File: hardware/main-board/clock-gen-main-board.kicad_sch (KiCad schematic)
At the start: 10 parts, among them J1 Conn_01x03_Pin, J2 Conn_01x03_Pin, J3 Conn_01x03_Pin, U1 Pico

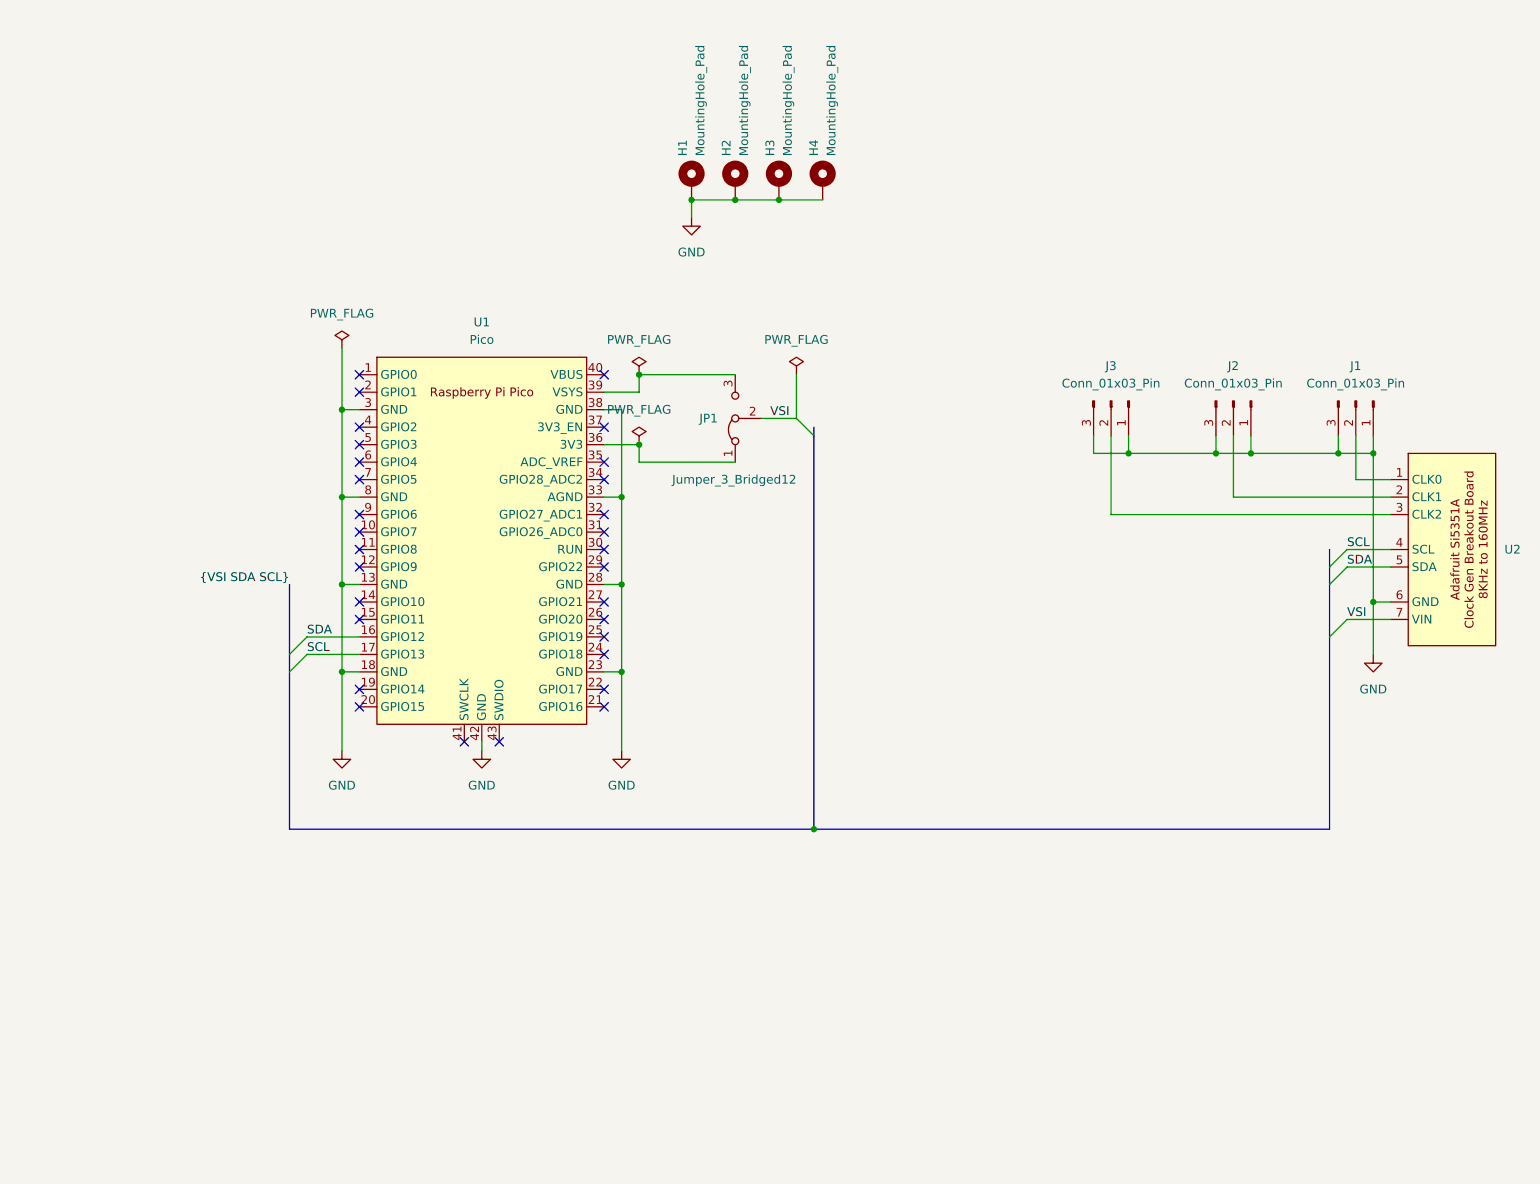
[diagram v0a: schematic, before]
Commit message: Resolve "Extend mainboard with audio ADC"
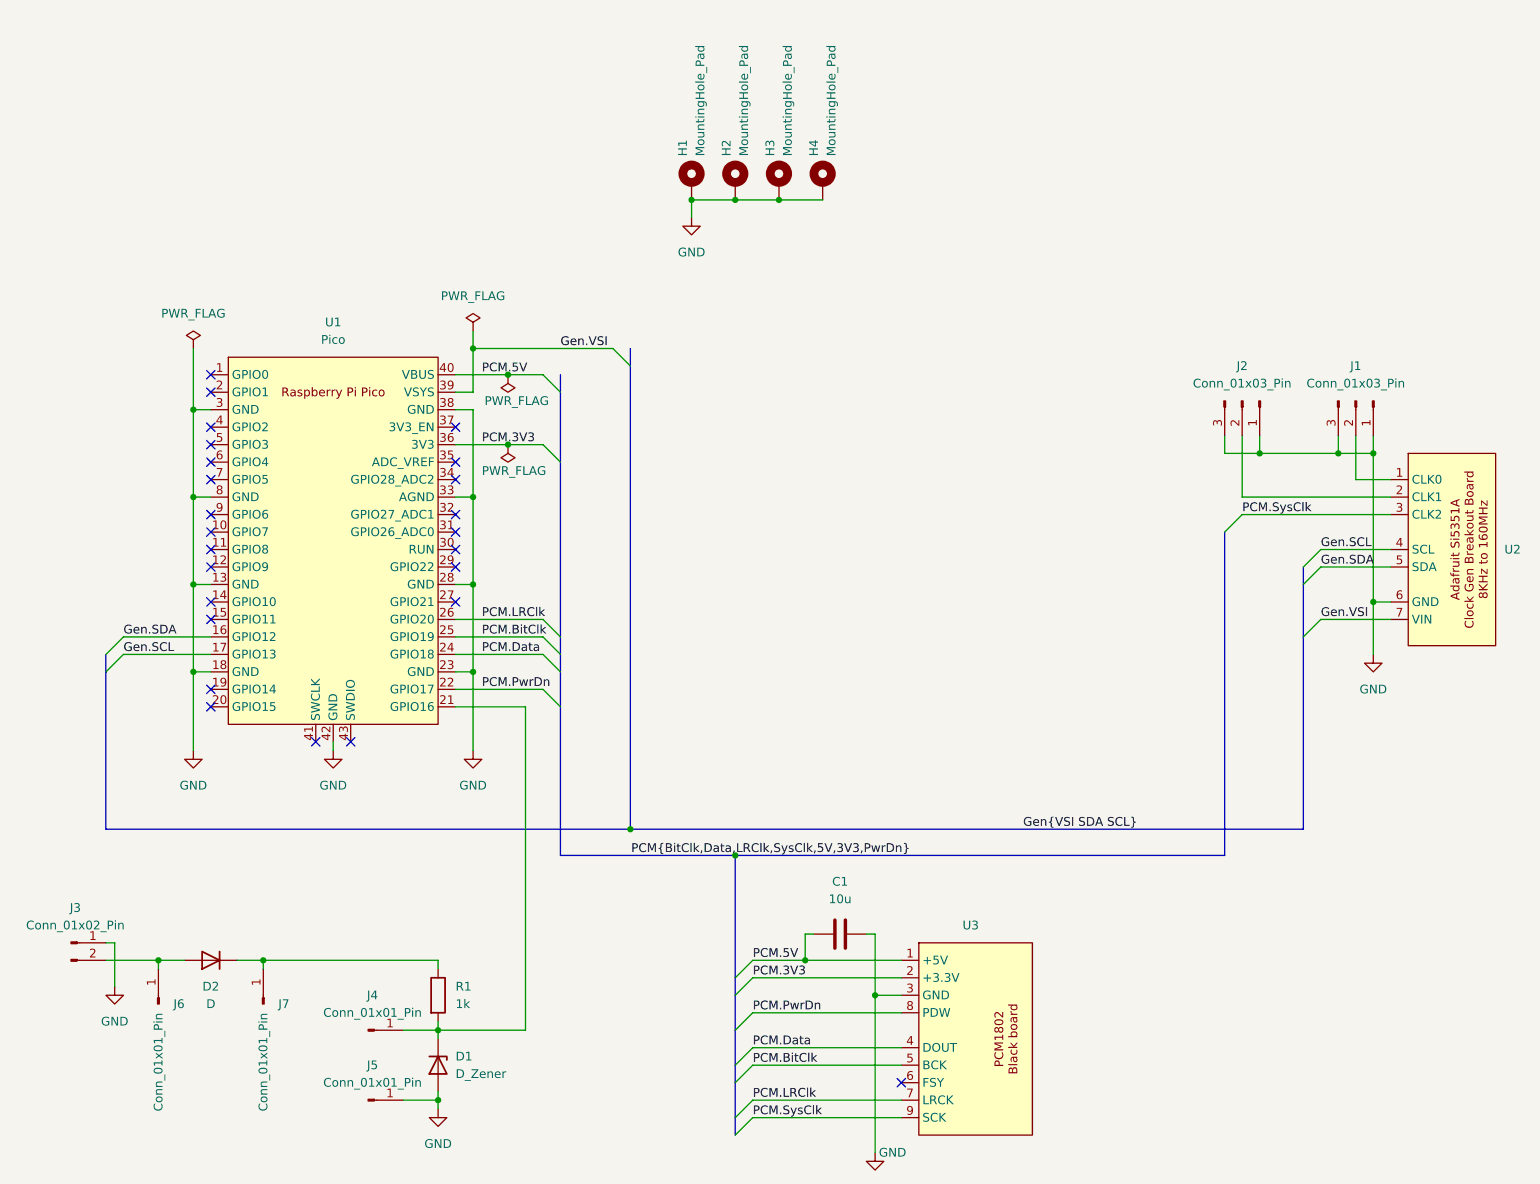
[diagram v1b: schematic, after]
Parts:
- removed J3: Conn_01x03_Pin, Connector_PinHeader_2.54mm:PinHeader_1x03_P2.54mm_Vertical, symbol Connector:Conn_01x03_Pin
- removed JP1: Jumper_3_Bridged12, Connector_PinHeader_2.54mm:PinHeader_1x03_P2.54mm_Vertical, symbol Jumper:Jumper_3_Bridged12
- added C1: 10u, Capacitor_SMD:C_0805_2012Metric_Pad1.18x1.45mm_HandSolder, symbol Device:C
- added D1: D_Zener, Diode_SMD:D_SOD-123, symbol Device:D_Zener
- added D2: D, Diode_SMD:D_SOD-123, symbol Device:D
- added J3: Conn_01x02_Pin, Connector_PinHeader_2.54mm:PinHeader_1x02_P2.54mm_Vertical, symbol Connector:Conn_01x02_Pin
- added J4, J5, J6, J7: Conn_01x01_Pin, Connector_PinHeader_2.54mm:PinHeader_1x01_P2.54mm_Vertical, symbol Connector:Conn_01x01_Pin
- added R1: 1k, Resistor_SMD:R_0805_2012Metric_Pad1.20x1.40mm_HandSolder, symbol Device:R
- added U3: ~, black-pcm1802:black-pcm1802-board, symbol black-pcm1802:black-pcm1802-board
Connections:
- net VSI is gone; now on net Gen.VSI: U2.7 (VIN)
- net GND: now also C1.2, D1.2 (A), J3.1 (Pin_1), J5.1 (Pin_1), U3.3 (GND)
- net PCM.3V3: now reaches U1.36 (3V3)
- net PCM.3V3: now also U3.2 (+3.3V)
- net Gen.VSI: now reaches U1.39 (VSYS)
- net PCM.SysClk: now reaches U2.3 (CLK2)
- net PCM.SysClk: now also U3.9 (SCK)
- net at U1.21 (GPIO16): now also D1.1 (K), J4.1 (Pin_1), R1.2
- net PCM.PwrDn: now reaches U1.22 (GPIO17)
- net PCM.PwrDn: now also U3.8 (PDW)
- net PCM.Data: now reaches U1.24 (GPIO18)
- net PCM.Data: now also U3.4 (DOUT)
- net PCM.BitClk: now reaches U1.25 (GPIO19)
- net PCM.BitClk: now also U3.5 (BCK)
- net PCM.LRClk: now reaches U1.26 (GPIO20)
- net PCM.LRClk: now also U3.7 (LRCK)
- net PCM.5V: now reaches U1.40 (VBUS)
- net PCM.5V: now also C1.1, U3.1 (+5V)
- net SCL renamed Gen.SCL
- net SDA renamed Gen.SDA
- new net: D2.1 (K), J7.1 (Pin_1), R1.1
- new net: D2.2 (A), J3.2 (Pin_2), J6.1 (Pin_1)
- no-connect marks 30 -> 25
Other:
- moved on the sheet: J2, U1

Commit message: fix iovdd
- create new gerbers
- create new render
- update readme
- update changelog
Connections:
- net PCM.3V3 is gone; now on net Gen.VSI: U1.36 (3V3), U3.2 (+3.3V)
- net Gen.VSI: no longer U1.39 (VSYS)
- no-connect marks 25 -> 26
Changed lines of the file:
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@@
   (title_block
     (title "${proj-title}")
-    (date "2023-09-10")
+    (date "2023-09-23")
     (rev "${proj-version}")
     (company "${proj-author}")
@@
   )
   (junction (at 77.47 162.56) (diameter 0) (color 0 0 0 0)
-  )
-  (junction (at 82.55 63.5) (diameter 0) (color 0 0 0 0)
   )
   (junction (at 213.36 78.74) (diameter 0) (color 0 0 0 0)
@@
   (no_connect (at 44.45 67.31))
   (no_connect (at 44.45 77.47))
+  (no_connect (at 80.01 69.85))
   (no_connect (at 44.45 113.03))
   (no_connect (at 44.45 80.01))
@@
     (stroke (width 0) (type default))
   )
-  (bus_entry (at 105.41 66.04) (size -2.54 -2.54)
+  (bus_entry (at 105.41 80.01) (size -2.54 -2.54)
     (stroke (width 0) (type default))
   )
@@
     (stroke (width 0) (type default))
   )
-  (wire (pts (xy 82.55 63.5) (xy 82.55 60.96))
-    (stroke (width 0) (type default))
-  )
   (wire (pts (xy 30.48 149.86) (xy 30.48 156.21))
     (stroke (width 0) (type default))
@@
     (stroke (width 0) (type default))
   )
-  (wire (pts (xy 80.01 69.85) (xy 82.55 69.85))
-    (stroke (width 0) (type default))
-  )
   (wire (pts (xy 123.19 172.72) (xy 144.78 172.72))
     (stroke (width 0) (type default))
@@
     (stroke (width 0) (type default))
   )
-  (bus (pts (xy 105.41 63.5) (xy 105.41 66.04))
-    (stroke (width 0) (type default))
-  )
   (wire (pts (xy 205.74 92.71) (xy 215.9 92.71))
     (stroke (width 0) (type default))
@@
     (stroke (width 0) (type default))
   )
-  (wire (pts (xy 82.55 69.85) (xy 82.55 63.5))
-    (stroke (width 0) (type default))
-  )
   (bus (pts (xy 120.65 137.16) (xy 191.77 137.16))
     (stroke (width 0) (type default) (color 255 0 255 1))
@@
     (stroke (width 0) (type default))
   )
-  (bus (pts (xy 95.25 67.31) (xy 95.25 69.85))
-    (stroke (width 0) (type default) (color 255 0 255 1))
-  )
   (bus (pts (xy 95.25 110.49) (xy 95.25 115.57))
     (stroke (width 0) (type default) (color 255 0 255 1))
@@
     (stroke (width 0) (type default) (color 255 0 255 1))
   )
+  (wire (pts (xy 92.71 77.47) (xy 102.87 77.47))
+    (stroke (width 0) (type default))
+  )
   (wire (pts (xy 62.23 120.65) (xy 62.23 121.92))
     (stroke (width 0) (type default))
@@
     (stroke (width 0) (type default))
   )
-  (bus (pts (xy 105.41 66.04) (xy 105.41 133.35))
+  (bus (pts (xy 105.41 80.01) (xy 105.41 133.35))
     (stroke (width 0) (type default))
   )
@@
     (stroke (width 0) (type default))
   )
-  (wire (pts (xy 82.55 63.5) (xy 102.87 63.5))
-    (stroke (width 0) (type default))
-  )
   (wire (pts (xy 213.36 78.74) (xy 213.36 100.33))
     (stroke (width 0) (type default))
@@
     (effects (font (size 1.27 1.27)) (justify left bottom))
   )
-  (label "Gen.VSI" (at 95.25 63.5 0) (fields_autoplaced)
+  (label "Gen.VSI" (at 96.52 77.47 0) (fields_autoplaced)
     (effects (font (size 1.27 1.27)) (justify left bottom))
   )
@@
         )
       )
-    )
-  )
-  (symbol (lib_id "power:PWR_FLAG") (at 82.55 60.96 0) (unit 1)
-    (in_bom yes) (on_board yes) (dnp no) (fields_autoplaced)
-    (property "Reference" "#FLG01" (at 82.55 59.055 0)
-      (effects (font (size 1.27 1.27)) hide)
-    )
-    (property "Value" "PWR_FLAG" (at 82.55 55.88 0)
-      (effects (font (size 1.27 1.27)))
-    )
-    (property "Footprint" "" (at 82.55 60.96 0)
-      (effects (font (size 1.27 1.27)) hide)
-    )
-    (property "Datasheet" "~" (at 82.55 60.96 0)
-      (effects (font (size 1.27 1.27)) hide)
-    )
-    (pin "1")
-    (instances
-      (project "clock-gen-main-board"
-        (path "/68213f1a-ef72-41ad-91ae-2233eec398f7"
-          (reference "#FLG01") (unit 1)
-        )
-      )

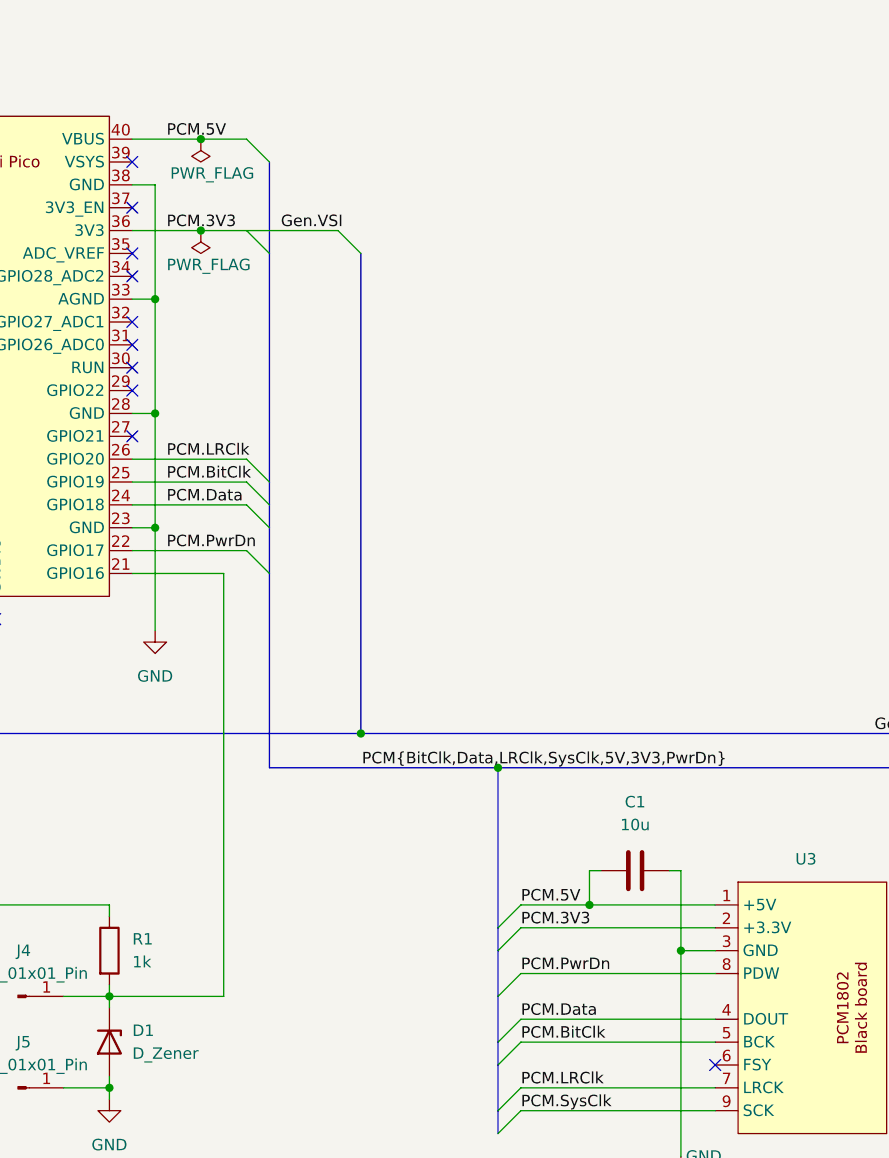
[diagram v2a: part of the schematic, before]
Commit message: Resolve "PCM1802 board 3.3V pin is driven instead of open"
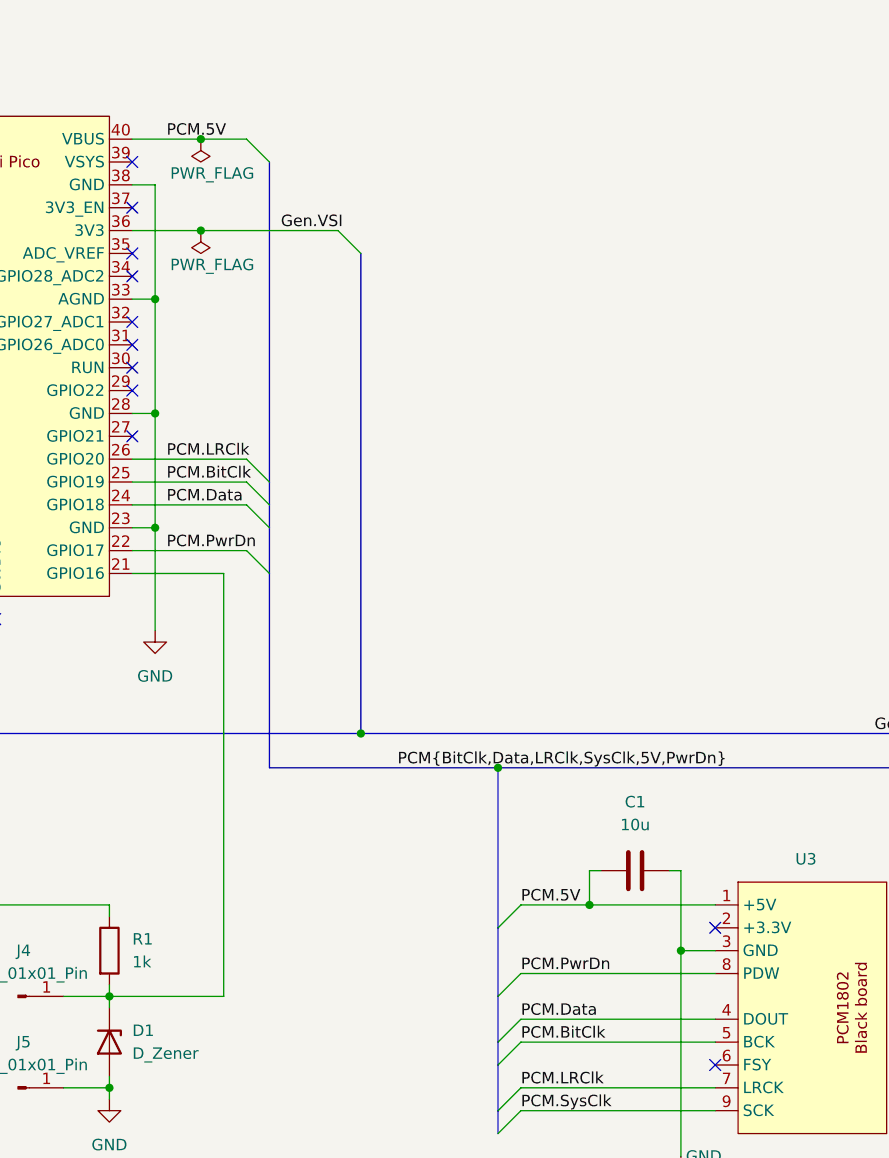
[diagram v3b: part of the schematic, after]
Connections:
- net Gen.VSI: no longer U3.2 (+3.3V)
- no-connect marks 26 -> 27
